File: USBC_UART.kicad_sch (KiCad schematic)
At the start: 6 parts, among them J15 USB_C, U5 CH340E

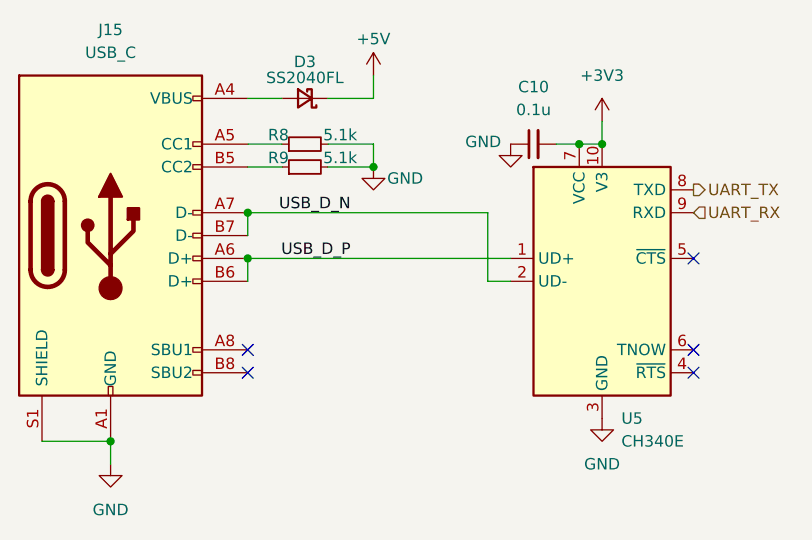
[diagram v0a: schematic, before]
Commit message: サーボと直接シリアル通信するためのUSB端子を追加、v0.1.1
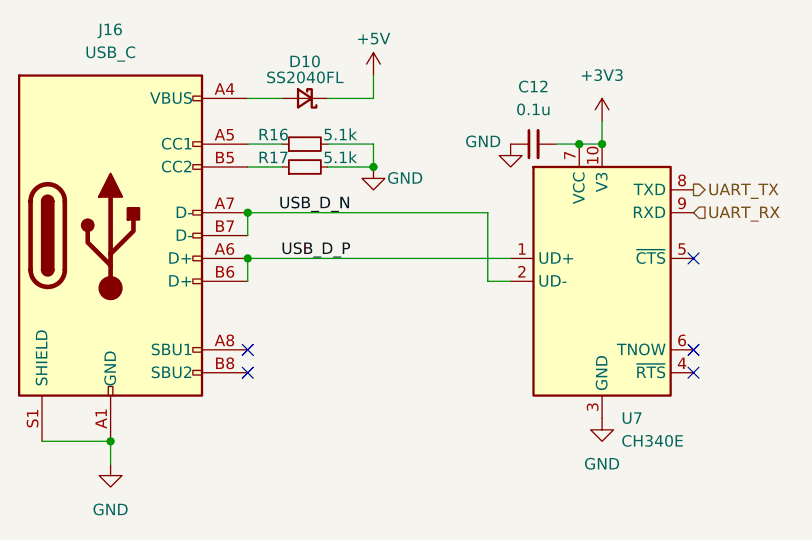
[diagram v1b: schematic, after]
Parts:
- renumbered C10 to C12, D3 to D10, J15 to J16, R8 to R16, R9 to R17, U5 to U7
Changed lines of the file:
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@@
 		(dnp no)
 		(fields_autoplaced yes)
-		(property "Reference" "C10"
+		(property "Reference" "C12"
 			(at 176.5363 59.69 90)
 			(effects
@@
 		(instances
 			(project "DRC-SerialSVMD2026"
+				(path "/b4b968b4-e169-4aaf-b6e2-cb81aeed17d9/536b2069-8c66-4216-849e-9d29241e6834"
+					(reference "C12")
+					(unit 1)
+				)
 				(path "/b4b968b4-e169-4aaf-b6e2-cb81aeed17d9/ec59fdac-f613-4295-94b0-c0a432fe0571"
 					(reference "C10")
@@
 		(dnp no)
 		(fields_autoplaced yes)
-		(property "Reference" "U5"
+		(property "Reference" "U7"
 			(at 186.2933 96.52 0)
 			(effects
@@
 		(instances
 			(project "DRC-SerialSVMD2026"
+				(path "/b4b968b4-e169-4aaf-b6e2-cb81aeed17d9/536b2069-8c66-4216-849e-9d29241e6834"
+					(reference "U7")
+					(unit 1)
+				)
 				(path "/b4b968b4-e169-4aaf-b6e2-cb81aeed17d9/ec59fdac-f613-4295-94b0-c0a432fe0571"
 					(reference "U5")
@@
 		(on_board yes)
 		(dnp no)
-		(property "Reference" "#PWR041"
+		(property "Reference" "#PWR057"
 			(at 158.75 62.23 0)
 			(effects
@@
 		(instances
 			(project "DRC-SerialSVMD2026"
+				(path "/b4b968b4-e169-4aaf-b6e2-cb81aeed17d9/536b2069-8c66-4216-849e-9d29241e6834"
+					(reference "#PWR057")
+					(unit 1)
+				)
 				(path "/b4b968b4-e169-4aaf-b6e2-cb81aeed17d9/ec59fdac-f613-4295-94b0-c0a432fe0571"
 					(reference "#PWR041")
@@
 		(on_board yes)
 		(dnp no)
-		(property "Reference" "D3"
+		(property "Reference" "D10"
 			(at 151.13 56.896 0)
 			(effects
@@
 		(instances
 			(project "DRC-SerialSVMD2026"
+				(path "/b4b968b4-e169-4aaf-b6e2-cb81aeed17d9/536b2069-8c66-4216-849e-9d29241e6834"
+					(reference "D10")
+					(unit 1)
+				)
 				(path "/b4b968b4-e169-4aaf-b6e2-cb81aeed17d9/ec59fdac-f613-4295-94b0-c0a432fe0571"
 					(reference "D3")
@@
 		(dnp no)
 		(fields_autoplaced yes)
-		(property "Reference" "J15"
+		(property "Reference" "J16"
 			(at 129.54 53.34 0)
 			(effects
@@
 		(instances
 			(project "DRC-SerialSVMD2026"
+				(path "/b4b968b4-e169-4aaf-b6e2-cb81aeed17d9/536b2069-8c66-4216-849e-9d29241e6834"
+					(reference "J16")
+					(unit 1)
+				)
 				(path "/b4b968b4-e169-4aaf-b6e2-cb81aeed17d9/ec59fdac-f613-4295-94b0-c0a432fe0571"
 					(reference "J15")
@@
 		(on_board yes)
 		(dnp no)
-		(property "Reference" "R8"
+		(property "Reference" "R16"
 			(at 149.352 65.024 90)
 			(effects
@@
 		(instances
 			(project "DRC-SerialSVMD2026"
+				(path "/b4b968b4-e169-4aaf-b6e2-cb81aeed17d9/536b2069-8c66-4216-849e-9d29241e6834"
+					(reference "R16")
+					(unit 1)
+				)
 				(path "/b4b968b4-e169-4aaf-b6e2-cb81aeed17d9/ec59fdac-f613-4295-94b0-c0a432fe0571"
 					(reference "R8")
@@
 		(on_board yes)
 		(dnp no)
-		(property "Reference" "R9"
+		(property "Reference" "R17"
 			(at 149.352 67.564 90)
 			(effects
@@
 		(instances
 			(project "DRC-SerialSVMD2026"
+				(path "/b4b968b4-e169-4aaf-b6e2-cb81aeed17d9/536b2069-8c66-4216-849e-9d29241e6834"
+					(reference "R17")
+					(unit 1)
+				)
 				(path "/b4b968b4-e169-4aaf-b6e2-cb81aeed17d9/ec59fdac-f613-4295-94b0-c0a432fe0571"
 					(reference "R9")
@@
 		(dnp no)
 		(fields_autoplaced yes)
-		(property "Reference" "#PWR044"
+		(property "Reference" "#PWR060"
 			(at 184.15 67.31 0)
 			(effects
@@
 		(instances
 			(project "DRC-SerialSVMD2026"
+				(path "/b4b968b4-e169-4aaf-b6e2-cb81aeed17d9/536b2069-8c66-4216-849e-9d29241e6834"
+					(reference "#PWR060")
+					(unit 1)
+				)
 				(path "/b4b968b4-e169-4aaf-b6e2-cb81aeed17d9/ec59fdac-f613-4295-94b0-c0a432fe0571"
 					(reference "#PWR044")
@@
 		(on_board yes)
 		(dnp no)
-		(property "Reference" "#PWR043"
+		(property "Reference" "#PWR059"
 			(at 173.99 72.39 0)
 			(effects
@@
 		(instances
 			(project "DRC-SerialSVMD2026"
+				(path "/b4b968b4-e169-4aaf-b6e2-cb81aeed17d9/536b2069-8c66-4216-849e-9d29241e6834"
+					(reference "#PWR059")
+					(unit 1)
+				)
 				(path "/b4b968b4-e169-4aaf-b6e2-cb81aeed17d9/ec59fdac-f613-4295-94b0-c0a432fe0571"
 					(reference "#PWR043")
@@
 		(dnp no)
 		(fields_autoplaced yes)
-		(property "Reference" "#PWR045"
+		(property "Reference" "#PWR061"
 			(at 184.15 102.87 0)
 			(effects
@@
 		(instances
 			(project "DRC-SerialSVMD2026"
+				(path "/b4b968b4-e169-4aaf-b6e2-cb81aeed17d9/536b2069-8c66-4216-849e-9d29241e6834"
+					(reference "#PWR061")
+					(unit 1)
+				)
 				(path "/b4b968b4-e169-4aaf-b6e2-cb81aeed17d9/ec59fdac-f613-4295-94b0-c0a432fe0571"
 					(reference "#PWR045")
@@
 		(on_board yes)
 		(dnp no)
-		(property "Reference" "#PWR042"
+		(property "Reference" "#PWR058"
 			(at 158.75 74.93 0)
 			(effects
@@
 		(instances
 			(project "DRC-SerialSVMD2026"
+				(path "/b4b968b4-e169-4aaf-b6e2-cb81aeed17d9/536b2069-8c66-4216-849e-9d29241e6834"
+					(reference "#PWR058")
+					(unit 1)
+				)
 				(path "/b4b968b4-e169-4aaf-b6e2-cb81aeed17d9/ec59fdac-f613-4295-94b0-c0a432fe0571"
 					(reference "#PWR042")
@@
 		(dnp no)
 		(fields_autoplaced yes)
-		(property "Reference" "#PWR040"
+		(property "Reference" "#PWR056"
 			(at 129.54 107.95 0)
 			(effects
@@
 		(instances
 			(project "DRC-SerialSVMD2026"
+				(path "/b4b968b4-e169-4aaf-b6e2-cb81aeed17d9/536b2069-8c66-4216-849e-9d29241e6834"
+					(reference "#PWR056")
+					(unit 1)
+				)
 				(path "/b4b968b4-e169-4aaf-b6e2-cb81aeed17d9/ec59fdac-f613-4295-94b0-c0a432fe0571"
 					(reference "#PWR040")
